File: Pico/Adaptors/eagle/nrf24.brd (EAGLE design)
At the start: 29.5 x 17.8 mm, 3 parts

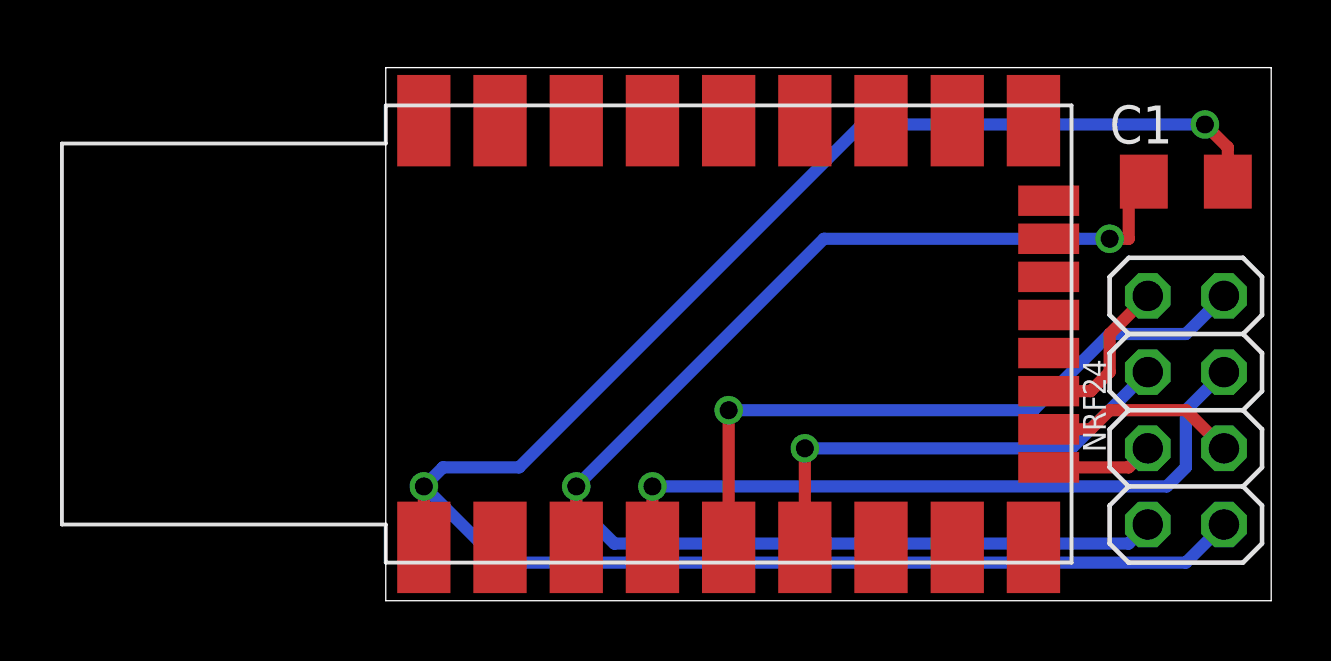
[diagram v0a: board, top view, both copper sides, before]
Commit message: updated NRF24, new Pico library part that does 0.1 holes and 0.05 SMD
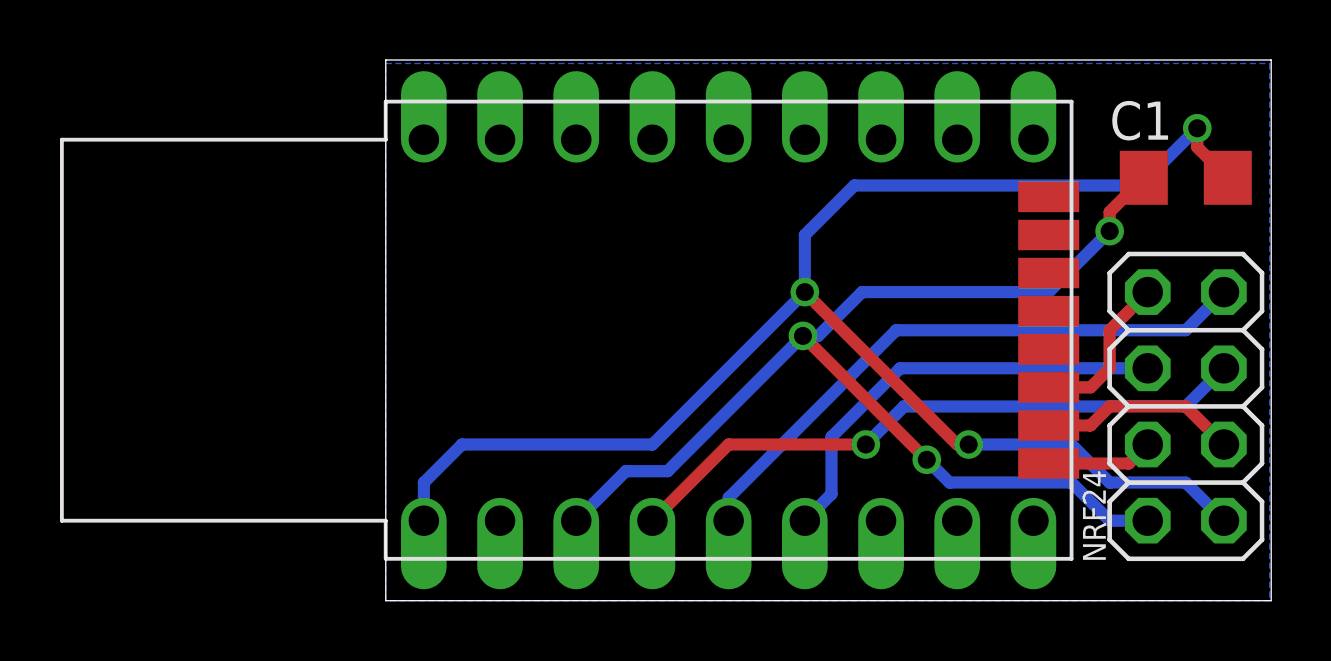
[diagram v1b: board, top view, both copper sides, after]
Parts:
- removed U$1: ESPRUINO_PICO_SMDONLY, espruino_pico:ESPRUINO_PICO_SMDONLY
- added U$2: ESPRUINO_PICO_HALFSMD, espruino_pico:ESPRUINO_PICO_HALFSMD
- moved NRF24 0.13 mm to (26.7, 6.48)
- moved C1 0.13 mm to (26.7, 14.1)
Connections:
- removed net N$1: C1.1, NRF24.2, U$1.3.3V
- removed net N$2: C1.2, NRF24.1, U$1.GND
- removed net N$4: NRF24.5, U$1.B3
- removed net N$5: NRF24.7, U$1.B4
- removed net N$6: NRF24.6, U$1.B5
- removed net N$7: NRF24.4, U$1.B8
- removed net N$8: NRF24.3, U$1.B9
- removed net N$9: NRF24.8, U$1.A10
- new net 3.3V: C1.1, NRF24.2, U$2.3.3V
- new net CE: NRF24.3, U$2.B9
- new net CSN: NRF24.4, U$2.B8
- new net GND: C1.2, NRF24.1, U$2.GND
- new net IRQ: NRF24.8, U$2.A10
- new net MISO: NRF24.7, U$2.B4
- new net MOSI: NRF24.6, U$2.B5
- new net SCK: NRF24.5, U$2.B3
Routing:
- net N$2: track 63.5 -> 0.00 mm, vias 2 -> 0
- net GND: track 0.00 -> 52.5 mm, vias 0 -> 3
- net N$1: track 46.5 -> 0.00 mm, vias 2 -> 0
- net 3.3V: track 0.00 -> 38.9 mm, vias 0 -> 3
- net N$4: track 23.8 -> 0.00 mm, vias 1 -> 0
- net N$5: track 22.7 -> 0.00 mm, vias 1 -> 0
- net SCK: track 0.00 -> 21.2 mm, vias 0 -> 1
- net MISO: track 0.00 -> 20.1 mm
- net N$6: track 15.8 -> 0.00 mm, vias 1 -> 0
- net MOSI: track 0.00 -> 14.7 mm
- net CE: track 0.00 -> 6.63 mm
- net N$8: track 6.63 -> 0.00 mm
- net N$9: track 5.36 -> 0.00 mm
- net IRQ: track 0.00 -> 5.36 mm
- net N$7: track 3.57 -> 0.00 mm
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- added copper zone on layer 16, net GND
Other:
- board size 29.5 x 17.8 mm -> 29.5 x 18 mm
